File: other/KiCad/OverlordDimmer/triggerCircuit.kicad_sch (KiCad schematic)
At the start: 12 parts, among them Q32 IRF740, Q34 2N3904, Q41 2N3906, Q42 IRF740, U11 4N25

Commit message: Final commit from laptop
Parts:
- C13: footprint Capacitor_SMD:C_0402_1005Metric_Pad0.74x0.62mm_HandSolder -> Capacitor_SMD:CP_Elec_3x5.4
- R55: footprint Resistor_SMD:R_1206_3216Metric_Pad1.30x1.75mm_HandSolder -> Resistor_SMD:R_0805_2012Metric_Pad1.20x1.40mm_HandSolder
- R58, R62: footprint Resistor_SMD:R_0402_1005Metric_Pad0.72x0.64mm_HandSolder -> Resistor_SMD:R_0805_2012Metric_Pad1.20x1.40mm_HandSolder
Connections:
- net L is gone; now on net Load: Q32.2 (D)
- net Load: no longer Q42.2 (D)
- new net N: Q42.2 (D)
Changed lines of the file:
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@@
     (stroke (width 0) (type default))
   )
-  (global_label "L" (shape input) (at 143.51 48.26 0) (fields_autoplaced)
+  (global_label "Load" (shape input) (at 143.51 48.26 0) (fields_autoplaced)
     (effects (font (size 1.27 1.27)) (justify left))
-    (property "Intersheetrefs" "${INTERSHEET_REFS}" (at 147.5233 48.26 0)
+    (property "Intersheetrefs" "${INTERSHEET_REFS}" (at 150.9703 48.26 0)
       (effects (font (size 1.27 1.27)) (justify left) hide)
     )
   )
-  (hierarchical_label "Load" (shape input) (at 143.51 83.82 0) (fields_autoplaced)
+  (hierarchical_label "N" (shape input) (at 143.51 83.82 0) (fields_autoplaced)
     (effects (font (size 1.27 1.27)) (justify left))
   )
@@
       (effects (font (size 1.27 1.27)) (justify right))
     )
-    (property "Footprint" "Resistor_SMD:R_0402_1005Metric_Pad0.72x0.64mm_HandSolder" (at 57.658 80.01 90)
+    (property "Footprint" "Resistor_SMD:R_0805_2012Metric_Pad1.20x1.40mm_HandSolder" (at 57.658 80.01 90)
       (effects (font (size 1.27 1.27)) hide)
     )
@@
       (effects (font (size 1.27 1.27)))
     )
-    (property "Footprint" "Resistor_SMD:R_1206_3216Metric_Pad1.30x1.75mm_HandSolder" (at 30.48 62.738 90)
+    (property "Footprint" "Resistor_SMD:R_0805_2012Metric_Pad1.20x1.40mm_HandSolder" (at 30.48 62.738 90)
       (effects (font (size 1.27 1.27)) hide)
     )
@@
       (effects (font (size 1.27 1.27)) (justify left))
     )
-    (property "Footprint" "Capacitor_SMD:C_0402_1005Metric_Pad0.74x0.62mm_HandSolder" (at 69.5452 83.82 0)
-      (effects (font (size 1.27 1.27)) hide)
-    )
-    (property "Datasheet" "https://si.farnell.com/yageo/cc0402mrx5r7bb475/cap-4-7f-16v-mlcc-0402/dp/3873408" (at 68.58 80.01 0)
+    (property "Footprint" "Capacitor_SMD:CP_Elec_3x5.4" (at 69.5452 83.82 0)
+      (effects (font (size 1.27 1.27)) hide)
+    )
+    (property "Datasheet" "https://www.mouser.se/ProductDetail/710-865090468011" (at 68.58 80.01 0)
       (effects (font (size 1.27 1.27)) hide)
     )
@@
       (effects (font (size 1.27 1.27)) (justify right))
     )
-    (property "Footprint" "Resistor_SMD:R_0402_1005Metric_Pad0.72x0.64mm_HandSolder" (at 122.428 81.28 90)
-      (effects (font (size 1.27 1.27)) hide)
-    )
+    (property "Footprint" "Resistor_SMD:R_0805_2012Metric_Pad1.20x1.40mm_HandSolder" (at 122.428 81.28 90)
+      (effects (font (size 1.27 1.27)) hide)
+    )

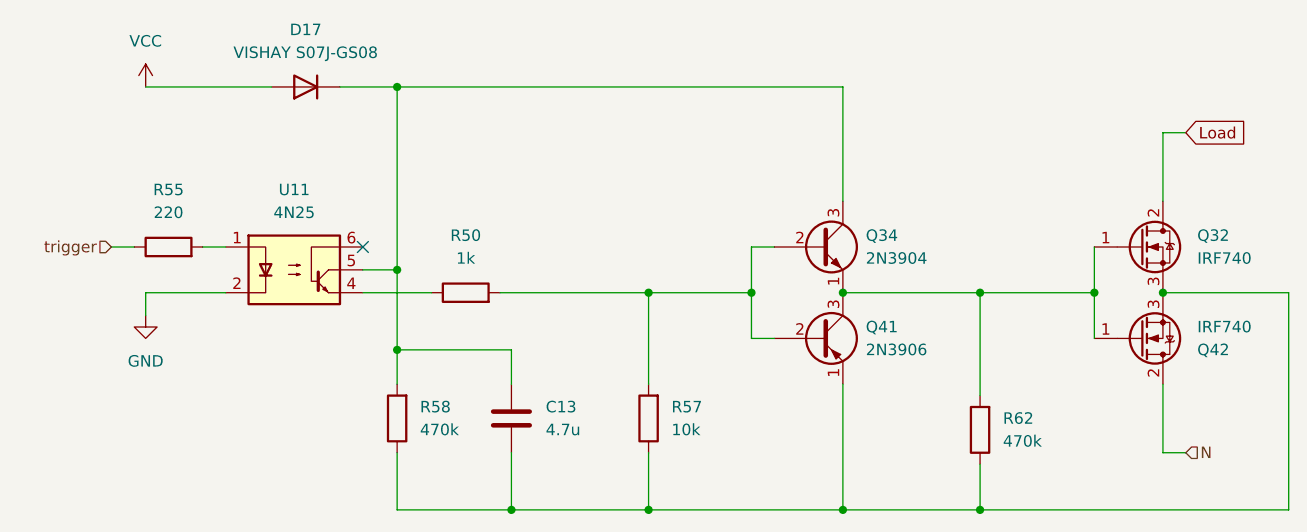
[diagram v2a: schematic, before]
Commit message: uploadable code, serial communication OK TODO: check pin and functionality compatibility
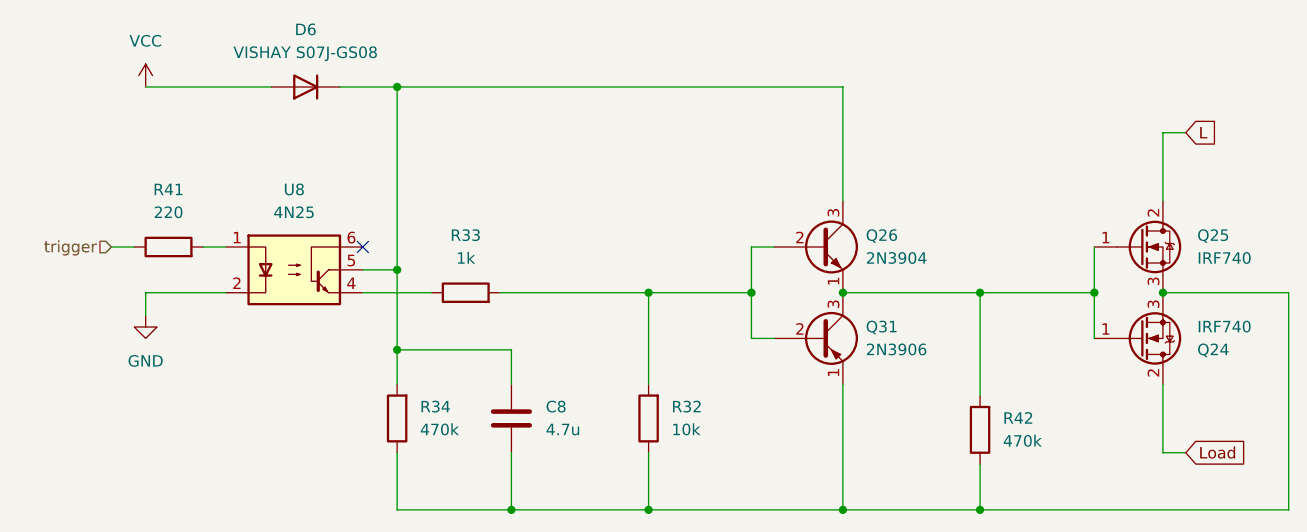
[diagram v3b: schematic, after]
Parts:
- C8: renamed from C13; footprint Capacitor_SMD:CP_Elec_3x5.4 -> Capacitor_SMD:C_1210_3225Metric_Pad1.33x2.70mm_HandSolder
- renumbered D17 to D6, Q42 to Q24, Q32 to Q25, Q34 to Q26, Q41 to Q31, R57 to R32, R50 to R33, R58 to R34, R55 to R41, R62 to R42, U11 to U8
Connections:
- net N is gone; now on net Load: Q24.2 (D)
- net Load: no longer Q25.2 (D)
- new net L: Q25.2 (D)

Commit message: Modified for S3 migration Prepared PCB for final inspection
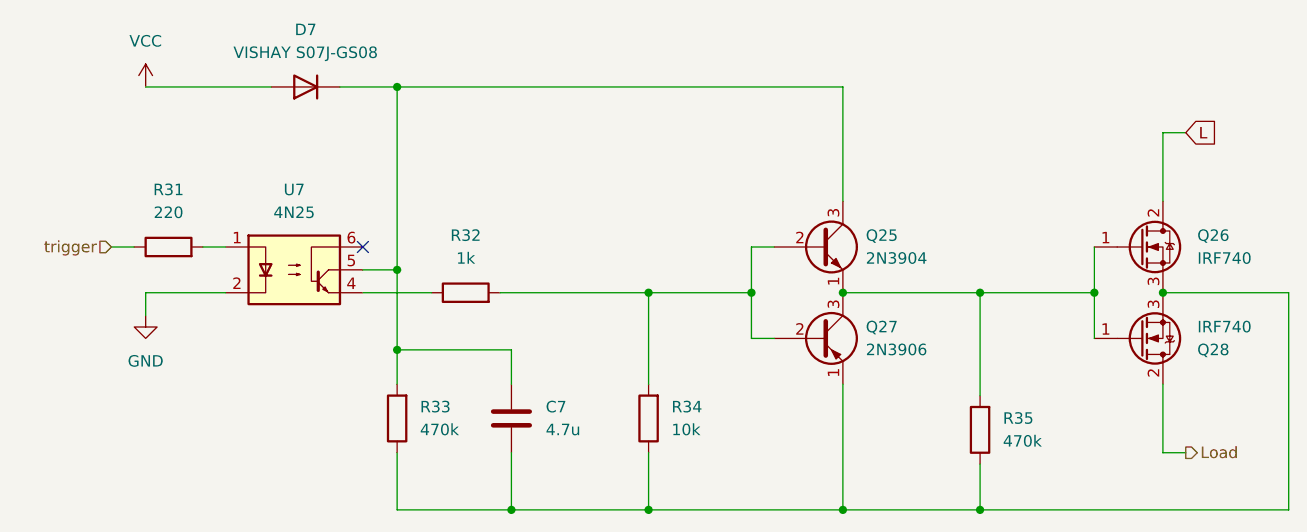
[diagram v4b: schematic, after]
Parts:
- renumbered C8 to C7, D6 to D7, Q26 to Q25, Q25 to Q26, Q31 to Q27, Q24 to Q28, R41 to R31, R33 to R32, R34 to R33, R32 to R34, R42 to R35, U8 to U7

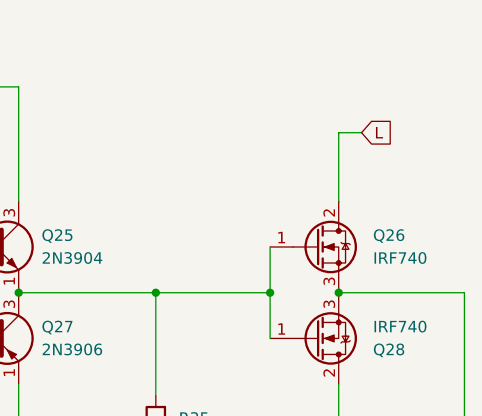
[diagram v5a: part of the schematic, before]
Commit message: Sent for PCB production, ver 1.2 rev A
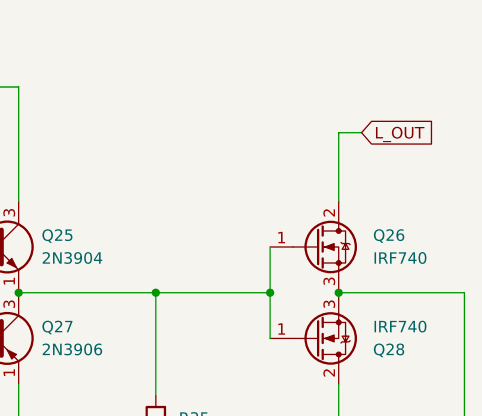
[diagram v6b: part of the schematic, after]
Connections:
- net L renamed L_OUT
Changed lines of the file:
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@@
 		)
 	)
-	(global_label "L"
+	(global_label "L_OUT"
 		(shape input)
 		(at 143.51 48.26 0)
@@
 		)
 		(property "Intersheetrefs" "${INTERSHEET_REFS}"
-			(at 147.5233 48.26 0)
+			(at 152.1195 48.26 0)
 			(effects
 				(font

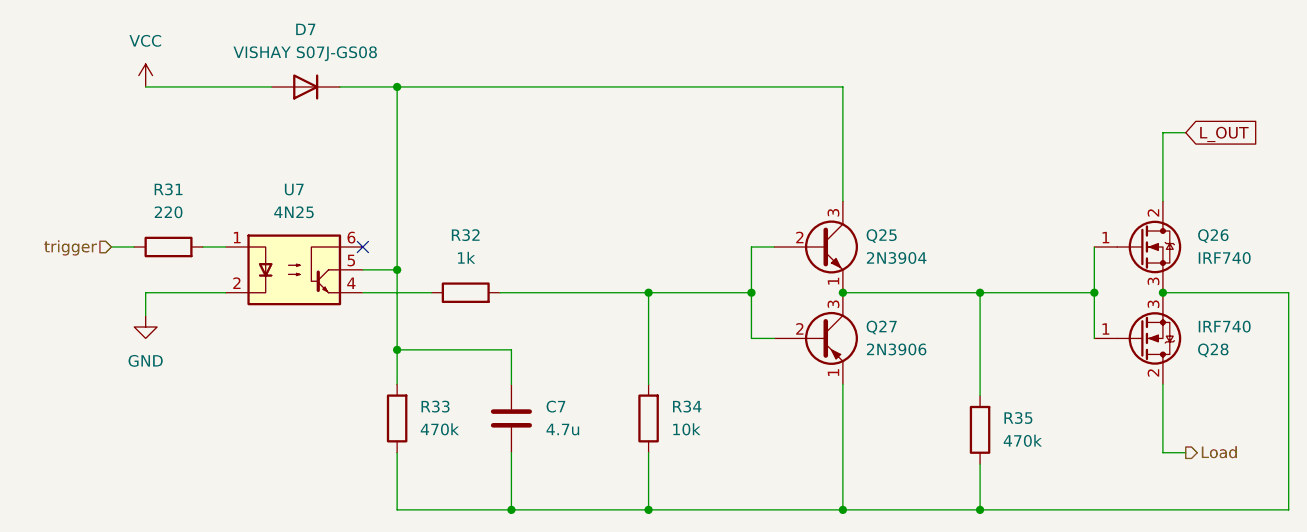
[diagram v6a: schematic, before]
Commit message: Updated PCB design - added pullup on boot pin GPIO0 - schematic cleanup - removed unused power supply parts
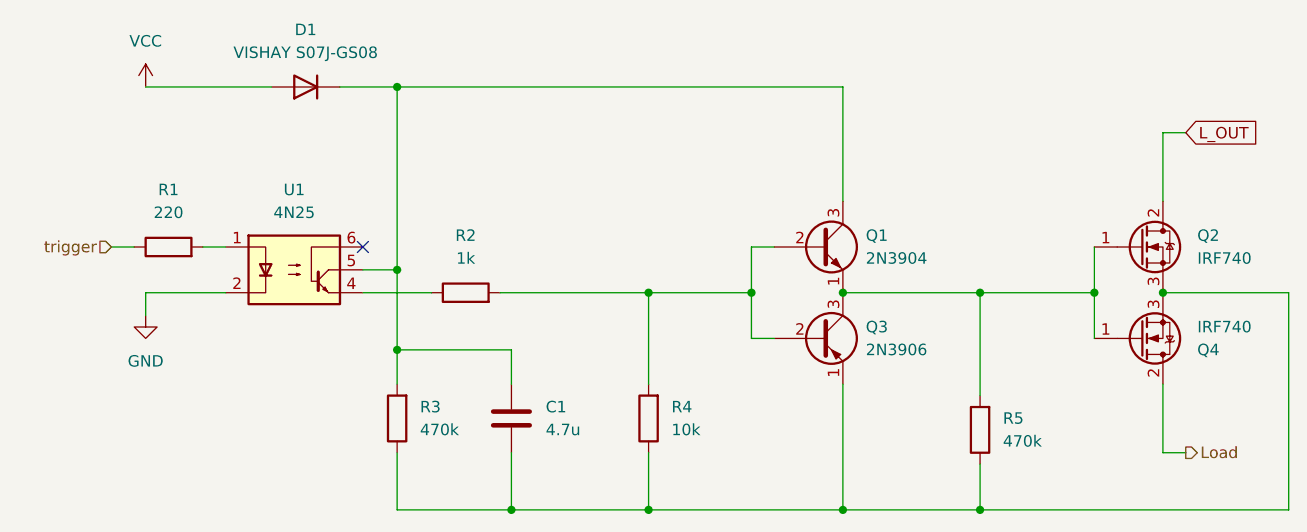
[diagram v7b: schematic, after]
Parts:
- renumbered C7 to C1, D7 to D1, Q25 to Q1, Q26 to Q2, Q27 to Q3, Q28 to Q4, R31 to R1, R32 to R2, R33 to R3, R34 to R4, R35 to R5, U7 to U1
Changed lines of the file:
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@@
 (kicad_sch
-	(version 20231120)
+	(version 20250114)
 	(generator "eeschema")
-	(generator_version "8.0")
+	(generator_version "9.0")
 	(paper "A4")
 	(junction
@@
 		(dnp no)
 		(fields_autoplaced yes)
-		(property "Reference" "#PWR021"
+		(property "Reference" "#PWR09"
 			(at 27.94 74.93 0)
 			(effects
@@
 		(dnp no)
 		(fields_autoplaced yes)
-		(property "Reference" "U7"
+		(property "Reference" "U1"
 			(at 44.45 54.61 0)
 			(effects
@@
 		(dnp no)
 		(fields_autoplaced yes)
-		(property "Reference" "R33"
+		(property "Reference" "R3"
 			(at 58.42 78.74 0)
 			(effects
@@
 		(dnp no)
 		(fields_autoplaced yes)
-		(property "Reference" "R31"
+		(property "Reference" "R1"
 			(at 30.48 54.61 90)
 			(effects
@@
 		(dnp no)
 		(fields_autoplaced yes)
-		(property "Reference" "Q26"
+		(property "Reference" "Q2"
 			(at 144.78 59.69 0)
 			(effects
@@
 		(dnp no)
 		(fields_autoplaced yes)
-		(property "Reference" "R32"
+		(property "Reference" "R2"
 			(at 63.5 59.69 90)
 			(effects
@@
 		(dnp no)
 		(fields_autoplaced yes)
-		(property "Reference" "Q25"
+		(property "Reference" "Q1"
 			(at 107.95 59.69 0)
 			(effects
@@
 		(dnp no)
 		(fields_autoplaced yes)
-		(property "Reference" "R34"
+		(property "Reference" "R4"
 			(at 86.36 78.74 0)
 			(effects
@@
 		(dnp no)
 		(fields_autoplaced yes)
-		(property "Reference" "C7"
+		(property "Reference" "C1"
 			(at 72.39 78.74 0)
 			(effects
@@
 		(dnp no)
 		(fields_autoplaced yes)
-		(property "Reference" "D7"
+		(property "Reference" "D1"
 			(at 45.72 36.83 0)
 			(effects
@@
 		(dnp no)
 		(fields_autoplaced yes)
-		(property "Reference" "Q27"
+		(property "Reference" "Q3"
 			(at 107.95 69.85 0)
 			(effects
@@
 		(dnp no)
 		(fields_autoplaced yes)
-		(property "Reference" "#PWR020"
+		(property "Reference" "#PWR08"
 			(at 27.94 46.99 0)
 			(effects
@@
 		(dnp no)
 		(fields_autoplaced yes)
-		(property "Reference" "R35"
+		(property "Reference" "R5"
 			(at 123.19 80.01 0)
 			(effects
@@
 		(on_board yes)
 		(dnp no)
-		(property "Reference" "Q28"
+		(property "Reference" "Q4"
 			(at 144.78 72.39 0)
 			(effects
